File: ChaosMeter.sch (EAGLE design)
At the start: 0 parts

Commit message: Added Caddock 1776-C6815 and diode array
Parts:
- added D1, D2, D3, D4, D5, D6: BAS116, SparkFun:DIODESOT23
- added D7: BAS70-04, diode:BAS70-04
- added U$1: CADDOCK-1776-C6815, CADDOCK-1776:CADDOCK-1776-C6815
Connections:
- new net N$1: D3.A, D4.C
- new net N$2: D2.C, D3.C, D6.C
- new net N$3: D1.A, D4.A, D5.A
- new net N$4: D5.C, D7.A1
- new net N$5: D6.A, D7.C2
- new net N$6: D7.C1A2
- new net N$7: D1.C, D2.A

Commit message: Added initial input protection, input divider switching and buffering
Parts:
- added C10, C11, C12, C13, C14, C15, C8, C9: 100n, rcl:C-EUC0603
- added C2, C3, C4, C5: 1µ, rcl:C-EUC0603
- added C6, C7: 1.5p, rcl:C-EUC0603
- added D10, D11, D12, D13, D8, D9: BAS116, SparkFun:DIODESOT23
- added D14: BAS70-04, diode:BAS70-04
- added F1, F2: FUSESH32, fuse:FUSESH32
- added F3, F4: (no value), discrete:ARRESTER
- added PAD1, PAD2, PAD3, PAD4: (no value), wirepad:2,54/1,1
- added R10, R6: 1.1k, varistor:THERMISTOR-5
- added R11, R12, R7, R8: S07K385, varistor:S07K385
- added R5, R9: 3.5k, rcl:R-EU_0613/15
- added U$2: EFM32GG232F1024, EnergyMicro:EFM32GG232F1024
- added U$3, U$4: CADDOCK-1776-C4815, CADDOCK-1776:CADDOCK-1776-C4815
- added U$5: CD74HC4316, AnalogSwitches:CD74HC4316
- added U$6, U$7: TLC2654A, AnalogSwitches:TLC2654A
- U$1: value CADDOCK-1776-C6815 -> CD74HC4316; device CADDOCK-1776:CADDOCK-1776-C6815 -> AnalogSwitches:CD74HC4316
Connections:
- new net +5V_CH1: C12.1, C13.1, U$1.VCC, U$7.V+
- new net +5V_CH2: C8.1, C9.1, U$5.VCC, U$6.V+
- new net -5V_CH1: C14.1, C15.1, C4.2, C5.2, U$1.VEE, U$7.V-
- new net -5V_CH2: C10.1, C11.1, C2.2, C3.2, U$5.VEE, U$6.V-
- new net FROM_INPUT_PROT_HI: R5.2, R7.1, U$3.P$1
- new net FROM_INPUT_PROT_HI2: R11.1, R9.2, U$4.P$1
- new net GND1: C12.2, C13.2, C14.2, C15.2, C7.2, D7.C1A2, F3.1, PAD2.P, R8.2, U$1.1Z, U$1.2Z, U$1.3Z, U$1.4Z, U$1.E, U$1.GND
- new net GND2: C10.2, C11.2, C6.2, C8.2, C9.2, D14.C1A2, F4.1, PAD4.P, R12.2, U$5.1Z, U$5.2Z, U$5.3Z, U$5.4Z, U$5.E, U$5.GND
- new net INPUT_JACK_HI: PAD1.P, R6.2
- new net INPUT_JACK_HI1: PAD3.P, R10.2
- new net INTEGRATOR_CH1: U$7.OUT
- new net INTEGRATOR_CH2: U$6.OUT
- new net N$10: D10.C, D13.C, D9.C
- new net N$11: U$1.2Y, U$3.P$4
- new net N$12: U$1.3Y, U$3.P$5
- new net N$13: U$1.4Y, U$3.P$6
- new net N$14: R11.2, R12.1
- new net N$15: U$1.1S
- new net N$16: U$1.2S
- new net N$17: U$1.3S
- new net N$18: U$1.4S
- new net N$19: D11.A, D12.A, D8.A
- new net N$20: D12.C, D14.A1
- new net N$21: R7.2, R8.1
- new net N$22: F4.2, R10.1, R9.1
- new net N$23: D13.A, D14.C2
- new net N$24: C6.1, D8.C, D9.A, U$4.P$2, U$4.P$7, U$6.+
- new net N$25: U$4.P$3, U$5.1Y
- new net N$26: U$4.P$4, U$5.2Y
- new net N$27: U$4.P$5, U$5.3Y
- new net N$28: U$4.P$6, U$5.4Y
- new net N$29: U$5.1S
- new net N$30: U$5.2S
- new net N$31: U$5.3S
- new net N$32: U$5.4S
- new net N$34: C2.1, U$6.CXA
- new net N$35: U$6.-
- new net N$37: C3.1, U$6.CXB
- new net N$41: U$7.-
- new net N$43: C4.1, U$7.CXA
- new net N$44: C5.1, U$7.CXB
- new net N$8: U$1.1Y, U$3.P$3
- new net N$9: F3.2, R5.1, R6.1
- net N$6: now also D10.A, D11.C; no longer D7.C1A2
- net N$7: now also C7.1, U$3.P$2, U$3.P$7, U$7.+
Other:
- note added: "Felicitus"
- note added: "Input Protection"
- note added: "Opamp Taken from the OSHW Multimeter Project Needs testing if it works as expected"
- note added: "Possible alternative: Vishay 2381 660 93034 (600V rated) We would need to go down to CAT III / CAT II 600V as well."
- note added: "Voltage Divider Switching and Input Buffer"

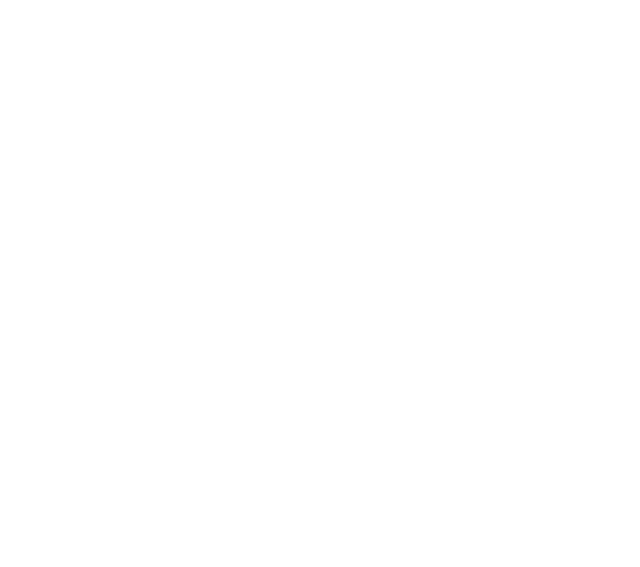
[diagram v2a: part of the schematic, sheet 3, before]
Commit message: Added note about the buttons for the front panel
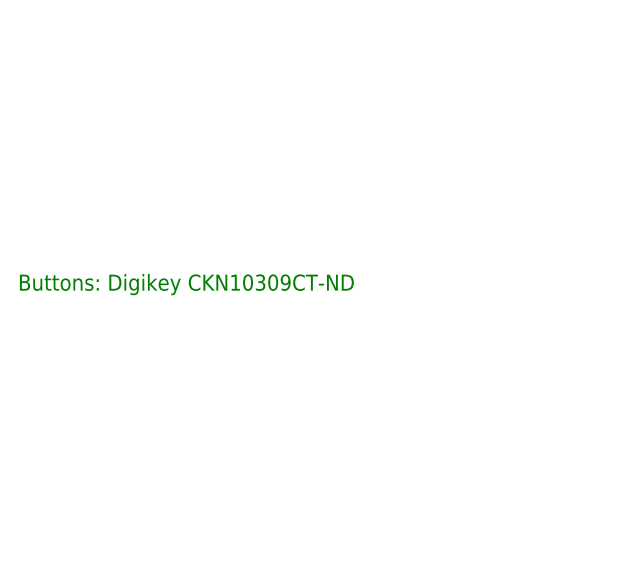
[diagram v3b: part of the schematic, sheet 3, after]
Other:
- note added: "Buttons: Digikey CKN10309CT-ND"
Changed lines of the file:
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@@
 <setting verticaltext="up"/>
 </settings>
-<grid distance="0.05" unitdist="inch" unit="inch" style="lines" multiple="1" display="no" altdistance="0.025" altunitdist="inch" altunit="inch"/>
+<grid distance="0.1" unitdist="inch" unit="inch" style="lines" multiple="1" display="no" altdistance="0.01" altunitdist="inch" altunit="inch"/>
 <layers>
 <layer number="1" name="Top" color="4" fill="1" visible="no" active="no"/>
@@
 <description>Display Section</description>
 <plain>
+<text x="55.88" y="139.7" size="1.778" layer="91">Buttons: Digikey CKN10309CT-ND</text>
 </plain>
 <instances>

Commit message: Added double fuses (11A/440mA) for the amps input
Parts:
- removed F1: FUSESH32, fuse:FUSESH32
- added AMPS1+, AMPS1-: (no value), wirepad:2,54/1,1
- added F5, F7: 11A, fuse:FUSESH32
- added F6: 440mA, fuse:FUSESH32
- F2: value FUSESH32 -> 440mA
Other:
- note added: "Amps Input"
- note added: "Input Protection Volts Ranges"
- note removed: "Input Protection"
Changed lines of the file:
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@@
 <?xml version="1.0" encoding="utf-8"?>
 <!DOCTYPE eagle SYSTEM "eagle.dtd">
-<eagle version="6.5.0">
+<eagle version="6.6.0">
 <drawing>
 <settings>
@@
 <part name="FRAME2" library="frames" deviceset="A4L-LOC" device=""/>
 <part name="U$2" library="EnergyMicro" deviceset="EFM32GG232F1024" device=""/>
-<part name="F1" library="fuse" deviceset="FUSE" device="SH32"/>
-<part name="F2" library="fuse" deviceset="FUSE" device="SH32"/>
 <part name="FRAME3" library="frames" deviceset="A4L-LOC" device=""/>
 <part name="R5" library="rcl" deviceset="R-EU_" device="0613/15" value="3.5k">
@@
 <part name="SUPPLY11" library="supply2" deviceset="GND1" device=""/>
 <part name="SUPPLY12" library="supply2" deviceset="GND1" device=""/>
+<part name="FRAME4" library="frames" deviceset="A4L-LOC" device=""/>
+<part name="AMPS1+" library="wirepad" deviceset="2,54/1,1" device=""/>
+<part name="AMPS1-" library="wirepad" deviceset="2,54/1,1" device=""/>
+<part name="F2" library="fuse" deviceset="FUSE" device="SH32" value="440mA"/>
+<part name="F5" library="fuse" deviceset="FUSE" device="SH32" value="11A"/>
+<part name="F6" library="fuse" deviceset="FUSE" device="SH32" value="440mA"/>
+<part name="F7" library="fuse" deviceset="FUSE" device="SH32" value="11A"/>
+<part name="FRAME5" library="frames" deviceset="A4L-LOC" device=""/>
 </parts>
 <sheets>
 <sheet>
 <plain>
+</plain>
+<instances>
+<instance part="FRAME5" gate="G$1" x="0" y="0"/>
+</instances>
+<busses>
+</busses>
+<nets>
+</nets>
+</sheet>
+<sheet>
+<plain>
 <text x="43.18" y="160.02" size="1.778" layer="91">Possible alternative: Vishay 2381 660 93034 (600V rated)
 We would need to go down to CAT III / CAT II 600V as well.</text>
-<text x="162.56" y="20.32" size="2.54" layer="94">Input Protection</text>
+<text x="162.56" y="22.86" size="2.54" layer="94" align="top-left">Input Protection
+Volts Ranges</text>
 <text x="217.17" y="20.32" size="2.54" layer="94">Felicitus</text>
 </plain>
@@
 </plain>
 <instances>
-<instance part="F1" gate="G$1" x="48.26" y="54.61"/>
-<instance part="F2" gate="G$1" x="48.26" y="64.77"/>
 </instances>
 <busses>
+</busses>
+<nets>
+</nets>
+</sheet>
+<sheet>
+<description>Amps Input</description>
+<plain>
+<text x="162.56" y="22.86" size="2.54" layer="94" align="top-left">Amps Input</text>
+</plain>
+<instances>
+<instance part="FRAME4" gate="G$1" x="0" y="0"/>
+<instance part="AMPS1+" gate="1" x="17.78" y="160.02"/>
+<instance part="AMPS1-" gate="1" x="17.78" y="132.08"/>
+<instance part="F2" gate="G$1" x="43.18" y="160.02"/>
+<instance part="F5" gate="G$1" x="43.18" y="152.4"/>
+<instance part="F6" gate="G$1" x="40.64" y="101.6"/>
+<instance part="F7" gate="G$1" x="40.64" y="93.98"/>
+</instances>
+<busses>
